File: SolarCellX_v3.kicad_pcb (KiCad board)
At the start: 6 copper layers, 48.4 x 48.4 mm, 56 parts, among them J1 XF2M-1015-1A, U2 Value, U3 TSL2561

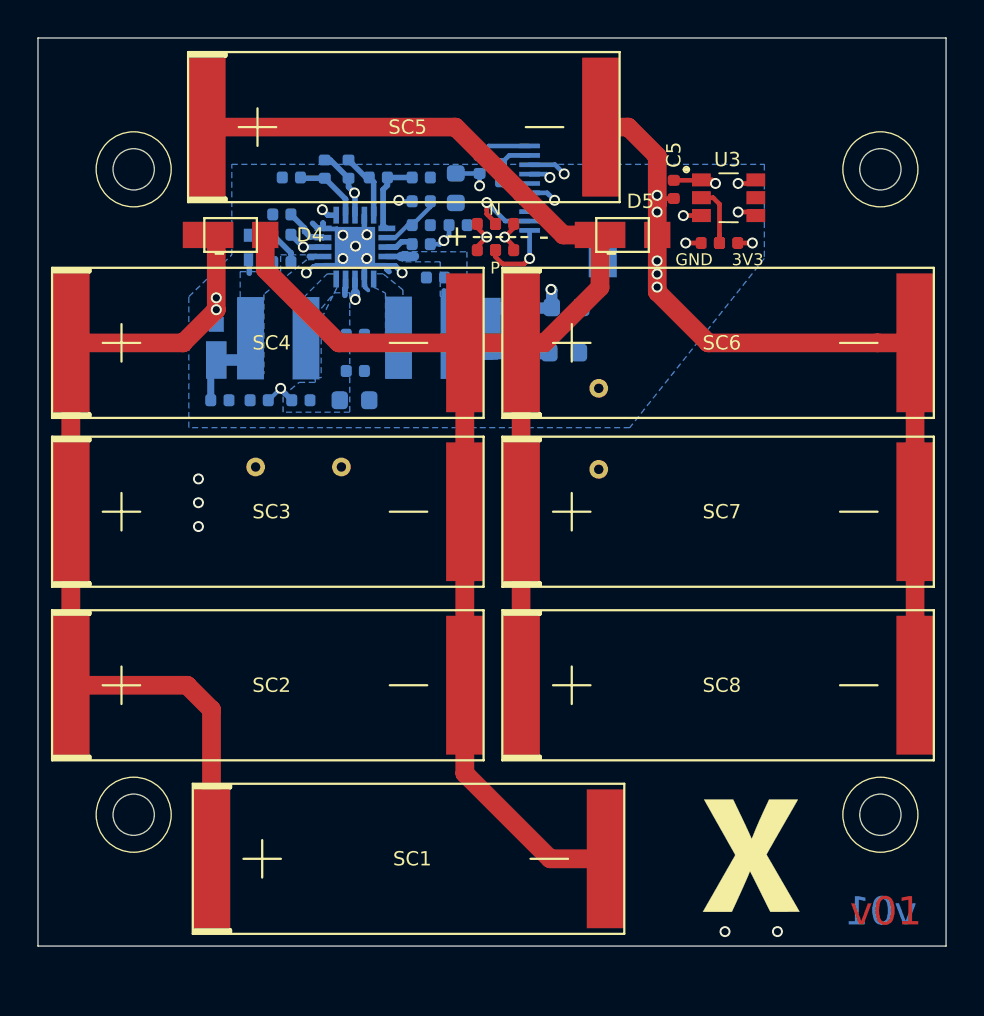
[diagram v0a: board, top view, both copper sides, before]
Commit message: fixed pcb - schematic inconsistencies
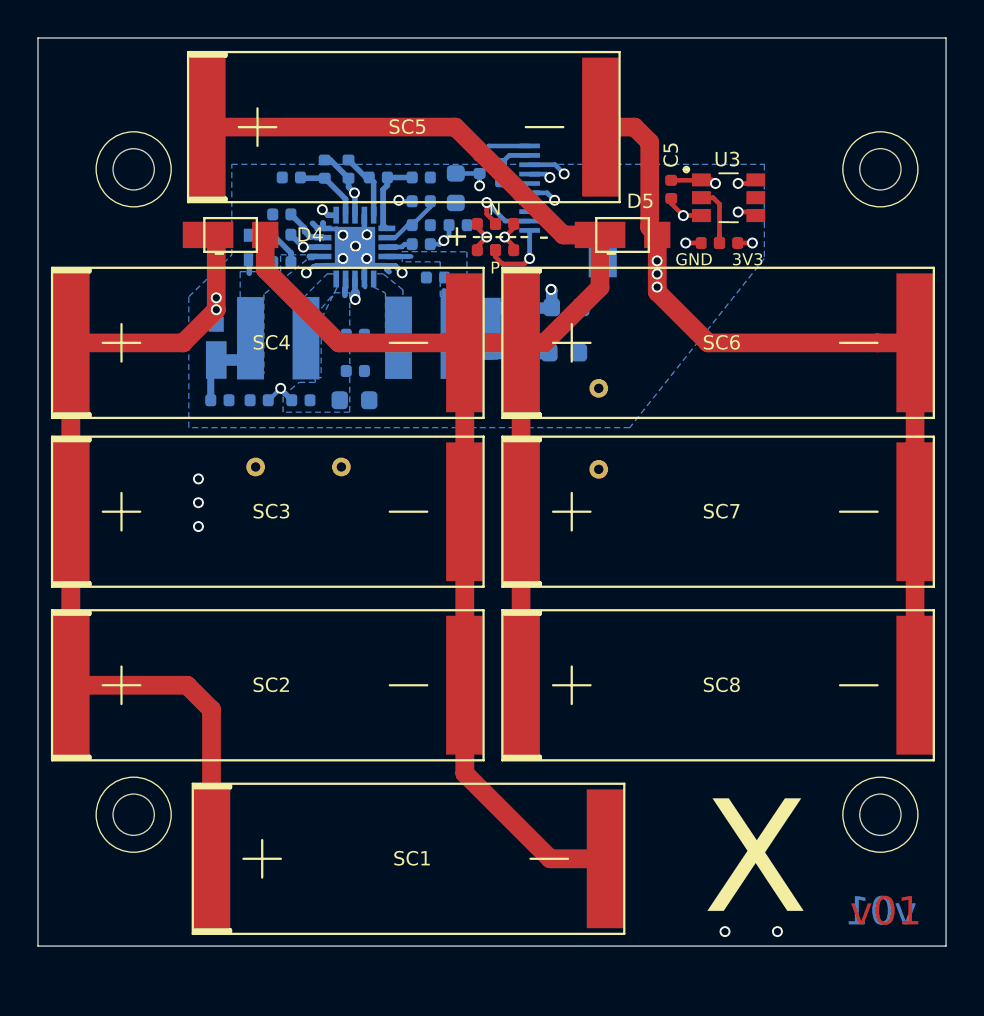
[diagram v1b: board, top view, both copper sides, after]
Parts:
- removed Ref**: Val**, custom-footprints:xpanel
- moved C5 0.14 mm to (123.8, 48.1)
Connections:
- net Net-(D3-Pad2) renamed /VSOLAR_FULL
- J1 pad 5: BURN1 -> (no net)
- U3 pad 5: Net-(U3-Pad5) -> (no net)
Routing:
- net Net-(C10-Pad1): track 9.20 -> 10.9 mm
- net VBAT_OK: track 1.52 -> 2.09 mm
- net GND: track 58.8 -> 59.0 mm, vias 14 -> 12
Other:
- net class Default: trace_width 0.2286 -> 0.127; via_dia 0.5842 -> 0.6; via_drill 0.381 -> 0.3
- rule trace_min: 0.1524 -> 0.127
- board text added: "X"

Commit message: moved solar panel and sun sensor. Fixed PCB design rules
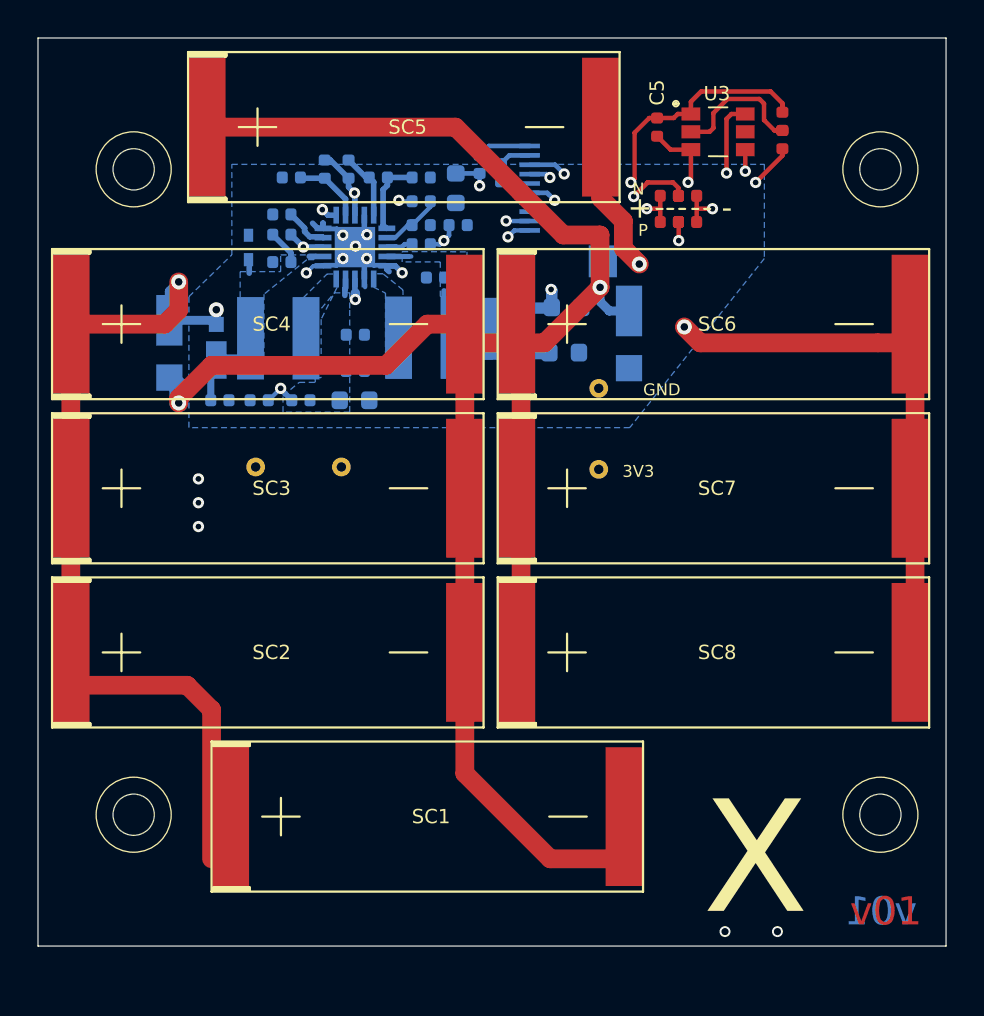
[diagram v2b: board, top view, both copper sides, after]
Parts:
- D4, D5: moved to B.Cu
- moved R19 9.86 mm to (124.6, 48.4)
- moved R2 9.86 mm to (123.7, 49.8)
- moved R3 9.86 mm to (124.6, 49.8)
- moved R4 9.86 mm to (123.7, 48.4)
- moved R12 7.09 mm to (129.7, 44.4), turned to 90 degrees
- moved R13 6.72 mm to (129.7, 45.4), turned to 90 degrees
- moved D4 6.61 mm to (97.0, 56.2), turned to 270 degrees
- moved D5 5.26 mm to (121.5, 55.8), turned to 270 degrees
- moved U3 3.56 mm to (126.2, 45.0)
- moved C5 3.40 mm to (123.0, 44.8)
- moved SC1 2.46 mm to (100.2, 81.5)
- moved SC8 1.77 mm to (115.5, 72.8)
- moved SC2 1.75 mm to (91.8, 72.8)
- moved SC7 1.27 mm to (115.5, 64.0)
- moved SC3 1.25 mm to (91.8, 64.0)
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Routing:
- net /coil: track 16389.4 -> 16417.0 mm
- net COIL_N: track 3.97 -> 15.5 mm, vias 1 -> 2
- net COIL_P: track 4.01 -> 11.7 mm, vias 1 -> 2
- net Net-(D4-Pad2): track 99.2 -> 106.4 mm, vias 0 -> 2
- net Net-(R12-Pad1): track 3.18 -> 7.28 mm
- net SDA1: track 12.8 -> 15.0 mm
- net GND: track 59.0 -> 57.5 mm, vias 12 -> 11
- net +3V3: track 37.6 -> 38.9 mm, vias 4 -> 3
- net /VSOLAR_FULL: track 57.6 -> 56.7 mm
